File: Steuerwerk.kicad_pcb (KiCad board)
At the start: 2 copper layers, 100 x 160 mm, 123 parts, among them J1 2PinTerminalBlocktg, J10 2PinTerminalBlocktg, J11 2PinTerminalBlocktg, J12 2PinTerminalBlocktg, J2 2PinTerminalBlocktg, J3 3PinTerminalBlocktg, J4 3PinTerminalBlocktg, J5 2PinTerminalBlocktg, J6 2PinTerminalBlocktg, J7 2PinTerminalBlocktg, J8 2PinTerminalBlocktg, J9 2PinTerminalBlocktg, Q1 Q_PNP_BCE, U1 74ls240, U2 74541, U3 74LS161, U4 74LS138, U5 74LS138, U6 74541, U7 74LS374, U8 74LS374

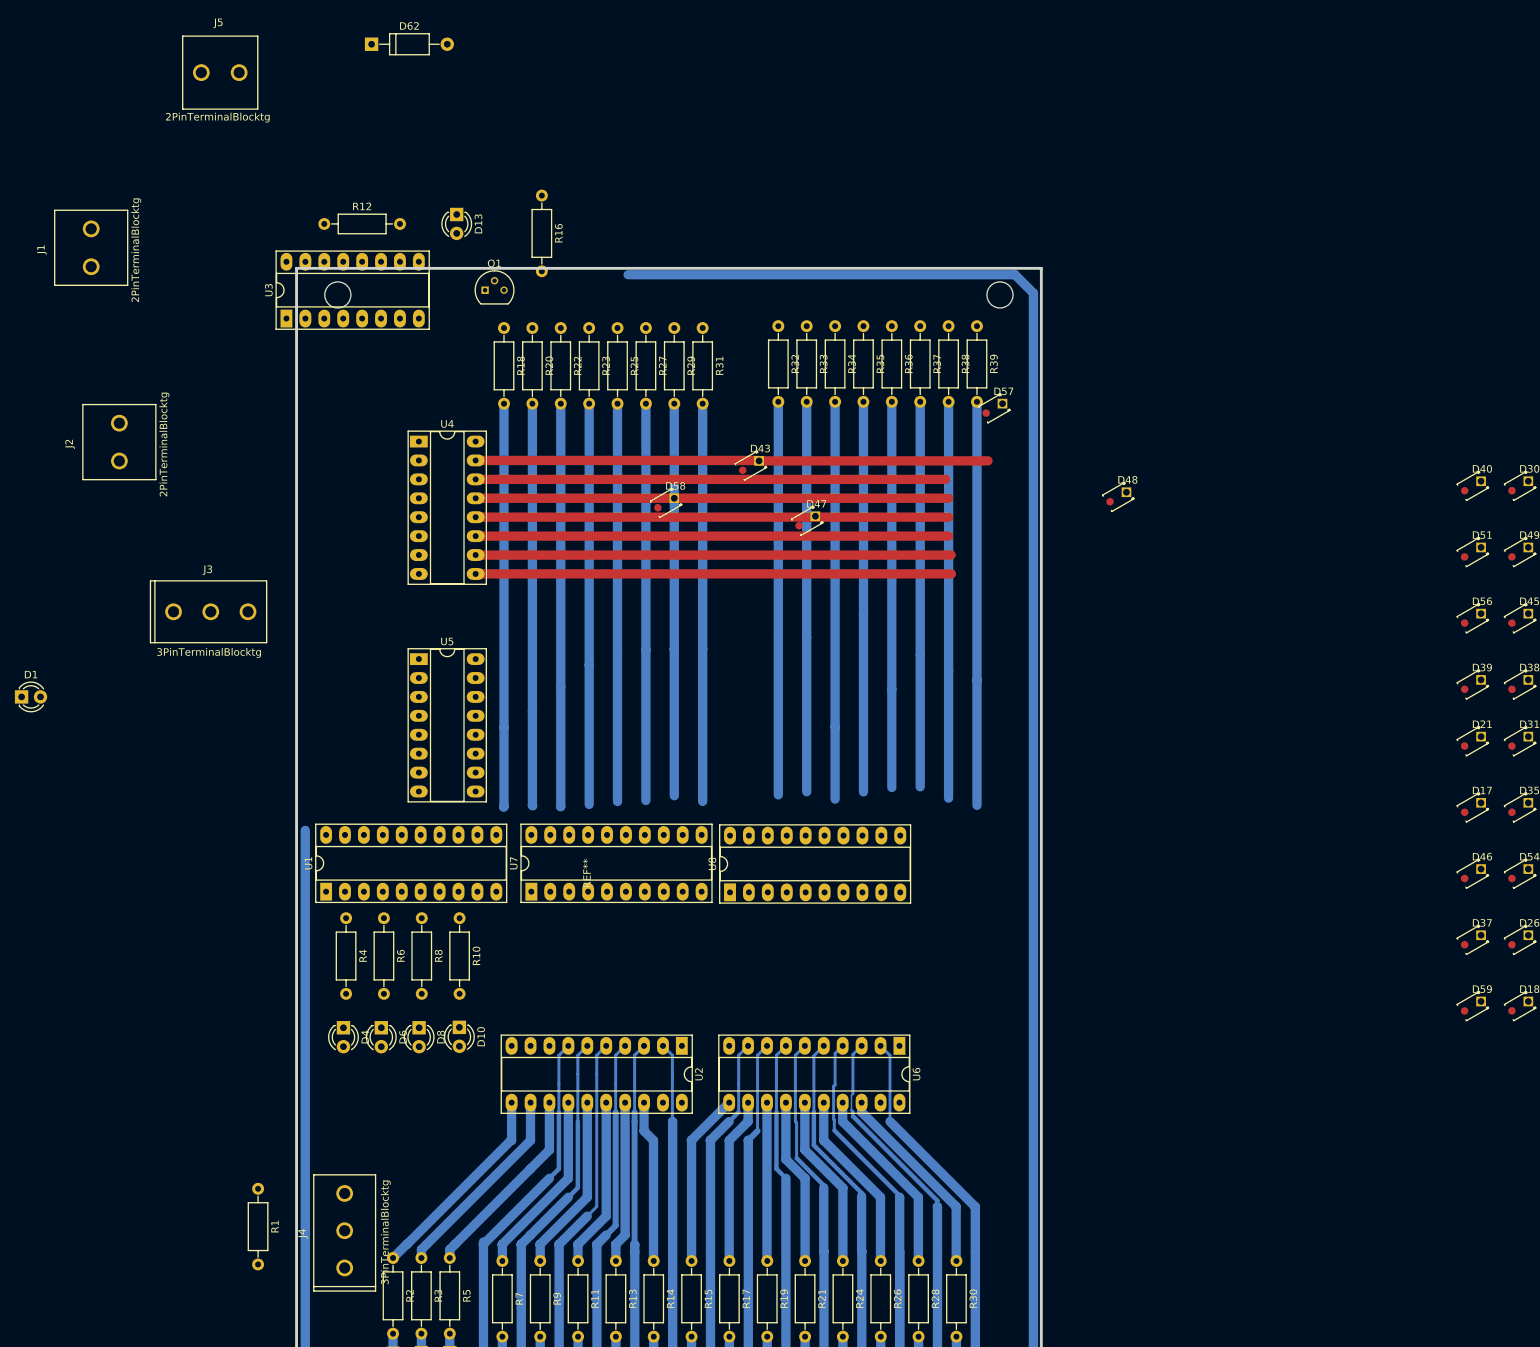
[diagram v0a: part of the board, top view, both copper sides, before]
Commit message: Teile verschoben, bahnen verlängert, Teile geordnet
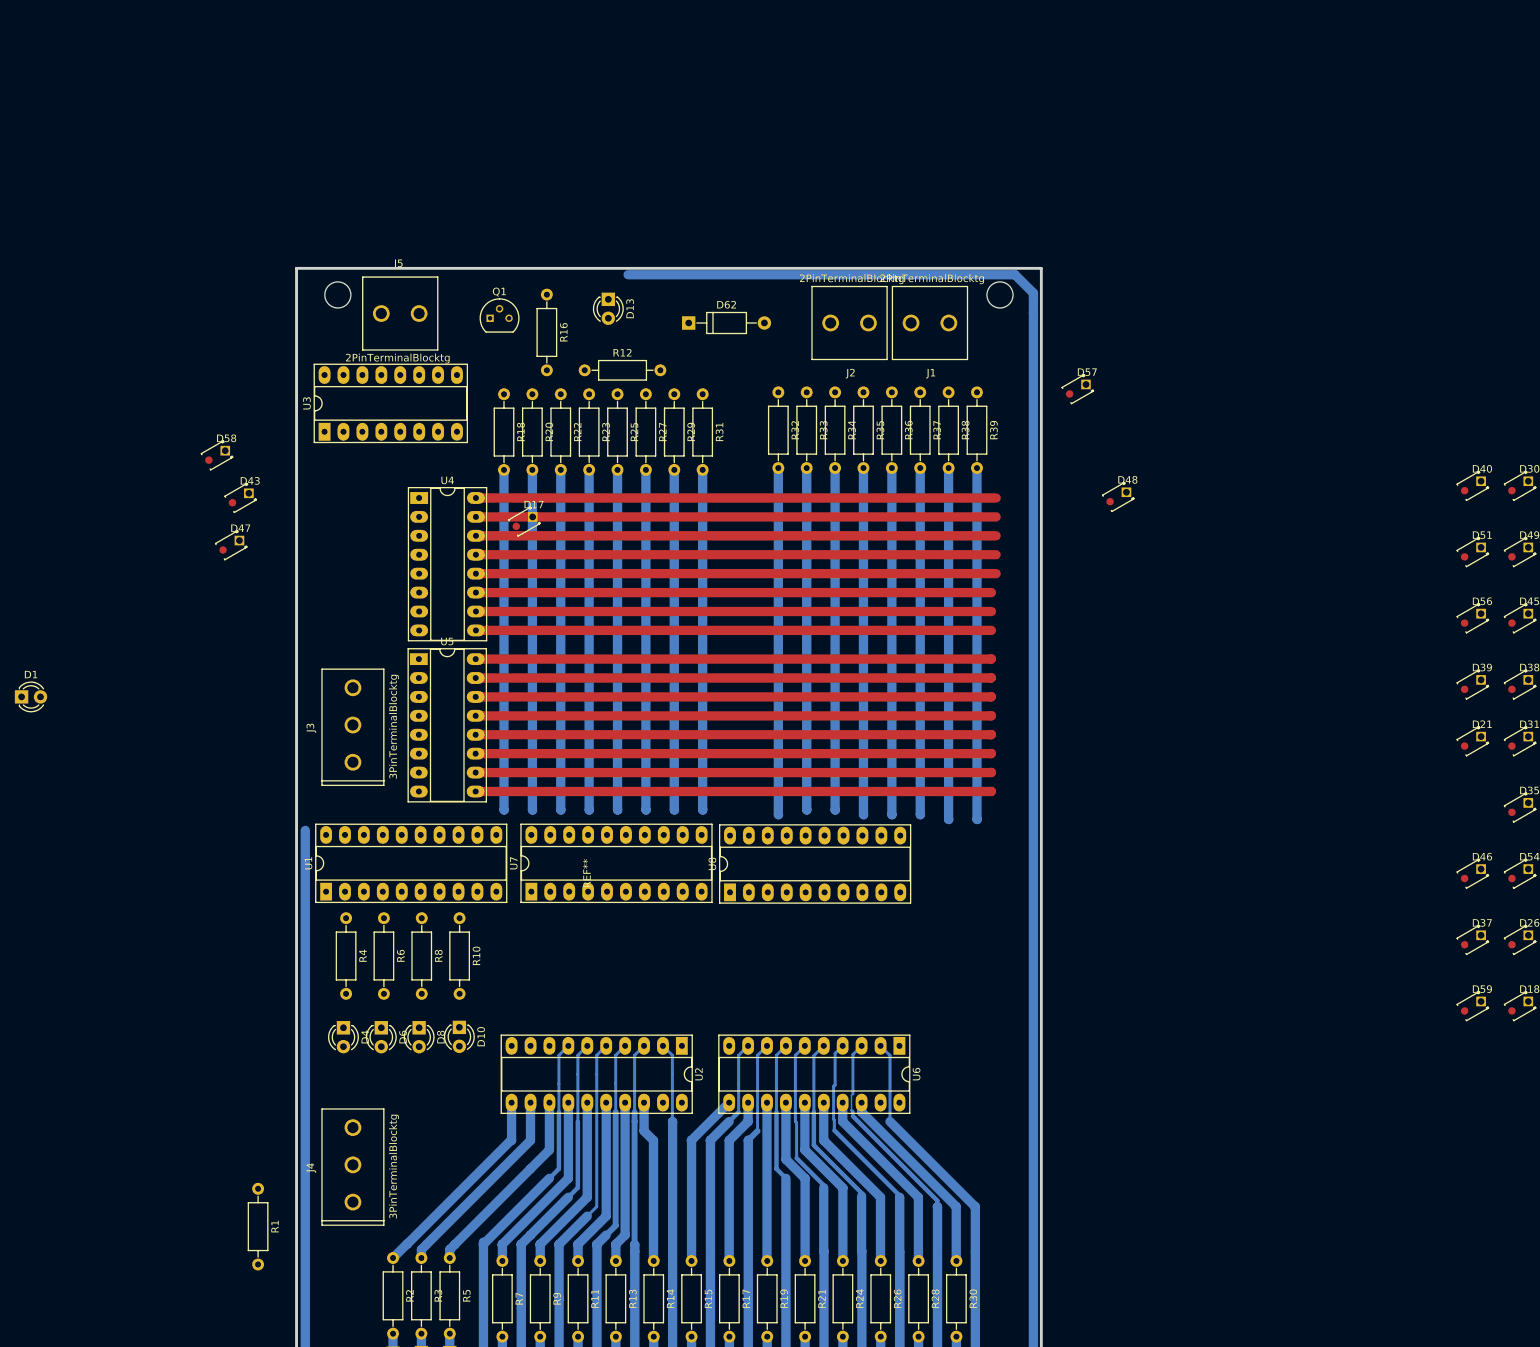
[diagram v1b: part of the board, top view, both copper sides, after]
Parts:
- moved D17 133.0 mm to (73.7, 77.4)
- moved J1 113.1 mm to (127.0, 51.4), turned to 180 degrees
- moved J2 99.3 mm to (116.2, 51.4), turned to 180 degrees
- moved D47 77.4 mm to (34.3, 80.6)
- moved D43 68.6 mm to (35.6, 74.3)
- moved D58 60.6 mm to (32.4, 68.5)
- moved D62 56.7 mm to (94.7, 51.4)
- moved J5 40.4 mm to (55.9, 50.1)
- moved R12 40.1 mm to (80.7, 57.7)
- moved J3 24.4 mm to (49.6, 105.4), turned to 90 degrees
- moved D13 23.3 mm to (83.9, 48.2)
- moved U3 16.0 mm to (45.8, 66.0)
- moved R16 13.3 mm to (75.6, 47.6)
- moved D57 11.5 mm to (148.0, 59.7)
- moved J4 8.91 mm to (49.6, 164.4)
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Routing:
- net VCC: track 639.5 -> 770.9 mm
- net Net-(D56-Pad1): track 0.00 -> 69.3 mm
- net Net-(D35-Pad1): track 0.00 -> 69.3 mm
- net Net-(D27-Pad1): track 0.00 -> 69.3 mm
- net Net-(D26-Pad1): track 0.00 -> 69.3 mm
- net Net-(D20-Pad1): track 0.00 -> 69.3 mm
- net Net-(D19-Pad1): track 0.00 -> 69.3 mm
- net Net-(D18-Pad1): track 0.00 -> 69.3 mm
- net Net-(D17-Pad2): track 54.2 -> 45.7 mm
- net Net-(D23-Pad2): track 54.1 -> 45.7 mm
- net Net-(D21-Pad2): track 54.0 -> 45.7 mm
- net Net-(D30-Pad2): track 53.8 -> 45.7 mm
- net Net-(D39-Pad2): track 53.4 -> 45.7 mm
- net Net-(R27-Pad2): track 53.3 -> 45.7 mm
- net Net-(D46-Pad2): track 53.4 -> 45.9 mm
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
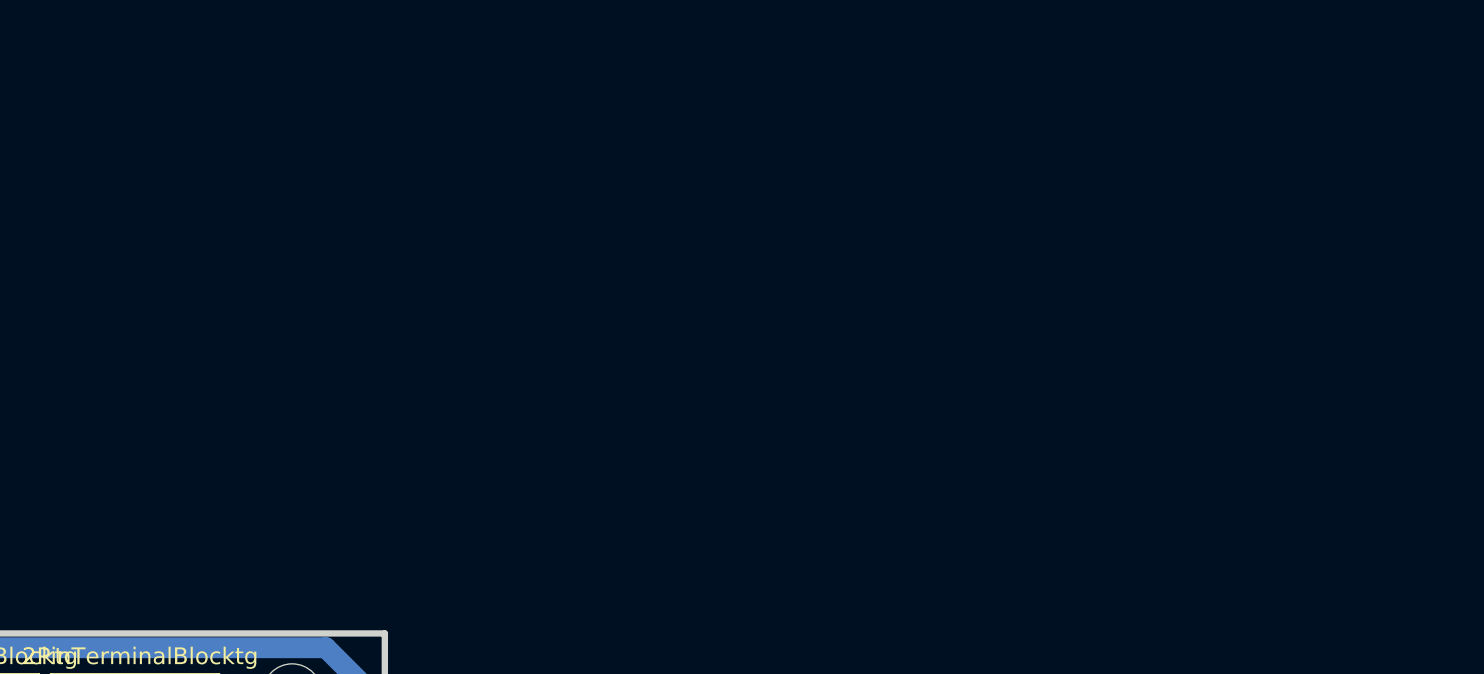
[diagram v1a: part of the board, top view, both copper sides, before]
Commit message: falsche ferbindung am lc374 korrigiert und rbussed eingefügt, condensatoren footprinted
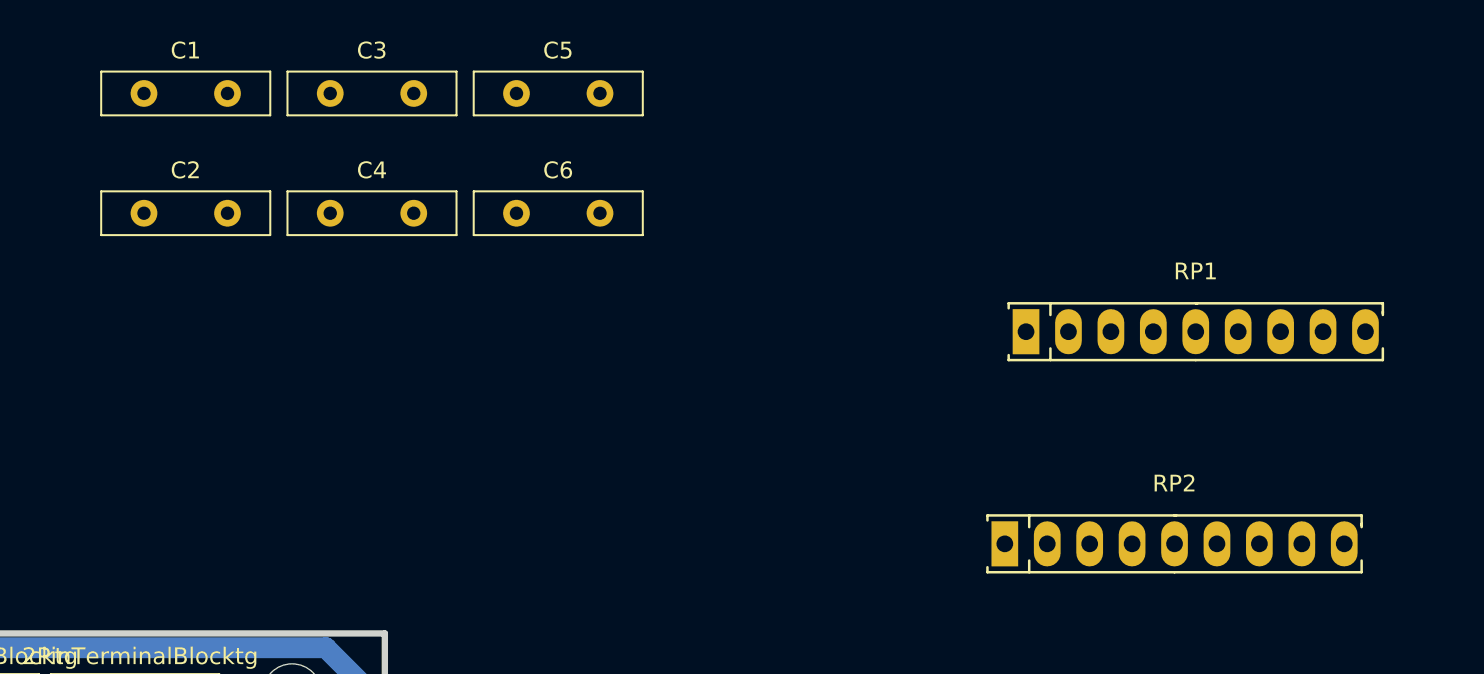
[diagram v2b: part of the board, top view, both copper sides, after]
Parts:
- added C1: 100n, Capacitors_ThroughHole:C_Disc_D10.0mm_W2.5mm_P5.00mm, F.Cu at (127.6, 11.7)
- added C2: 100n, Capacitors_ThroughHole:C_Disc_D10.0mm_W2.5mm_P5.00mm, F.Cu at (127.6, 18.9)
- added C3: 100n, Capacitors_ThroughHole:C_Disc_D10.0mm_W2.5mm_P5.00mm, F.Cu at (138.7, 11.7)
- added C4: 100n, Capacitors_ThroughHole:C_Disc_D10.0mm_W2.5mm_P5.00mm, F.Cu at (138.7, 18.9)
- added C5: 100n, Capacitors_ThroughHole:C_Disc_D10.0mm_W2.5mm_P5.00mm, F.Cu at (149.9, 11.7)
- added C6: 100n, Capacitors_ThroughHole:C_Disc_D10.0mm_W2.5mm_P5.00mm, F.Cu at (149.9, 18.9)
- added RP1: R_PACK8BUSSED, Housings_SIP:SIP9_Housing_BigPads, F.Cu at (190.5, 26.0)
- added RP2: R_PACK8BUSSED, Housings_SIP:SIP9_Housing_BigPads, F.Cu at (189.3, 38.7)
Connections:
- U7 pad 13: VCC -> Net-(D37-Pad2)
- U7 pad 14: Net-(R27-Pad2) -> VCC
- U7 pad 17: Net-(D37-Pad2) -> Net-(D23-Pad2)
- U7 pad 18: Net-(D39-Pad2) -> Net-(D17-Pad2)
- U7 pad 3: Net-(D17-Pad2) -> Net-(D21-Pad2)
- U7 pad 4: Net-(D21-Pad2) -> Net-(D30-Pad2)
- U7 pad 7: Net-(D23-Pad2) -> Net-(R27-Pad2)
- U7 pad 8: Net-(D30-Pad2) -> Net-(D39-Pad2)
- U8 pad 13: Net-(D59-Pad2) -> Net-(R38-Pad2)
- U8 pad 14: Net-(D61-Pad2) -> Net-(D59-Pad2)
- U8 pad 17: Net-(R38-Pad2) -> Net-(D47-Pad2)
- U8 pad 18: Net-(R39-Pad2) -> /Takt
- U8 pad 3: /Takt -> Net-(D43-Pad2)
- U8 pad 4: Net-(D43-Pad2) -> Net-(D46-Pad2)
- U8 pad 7: Net-(D47-Pad2) -> Net-(D61-Pad2)
- U8 pad 8: Net-(D46-Pad2) -> Net-(R39-Pad2)
